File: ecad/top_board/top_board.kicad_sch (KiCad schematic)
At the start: 0 parts

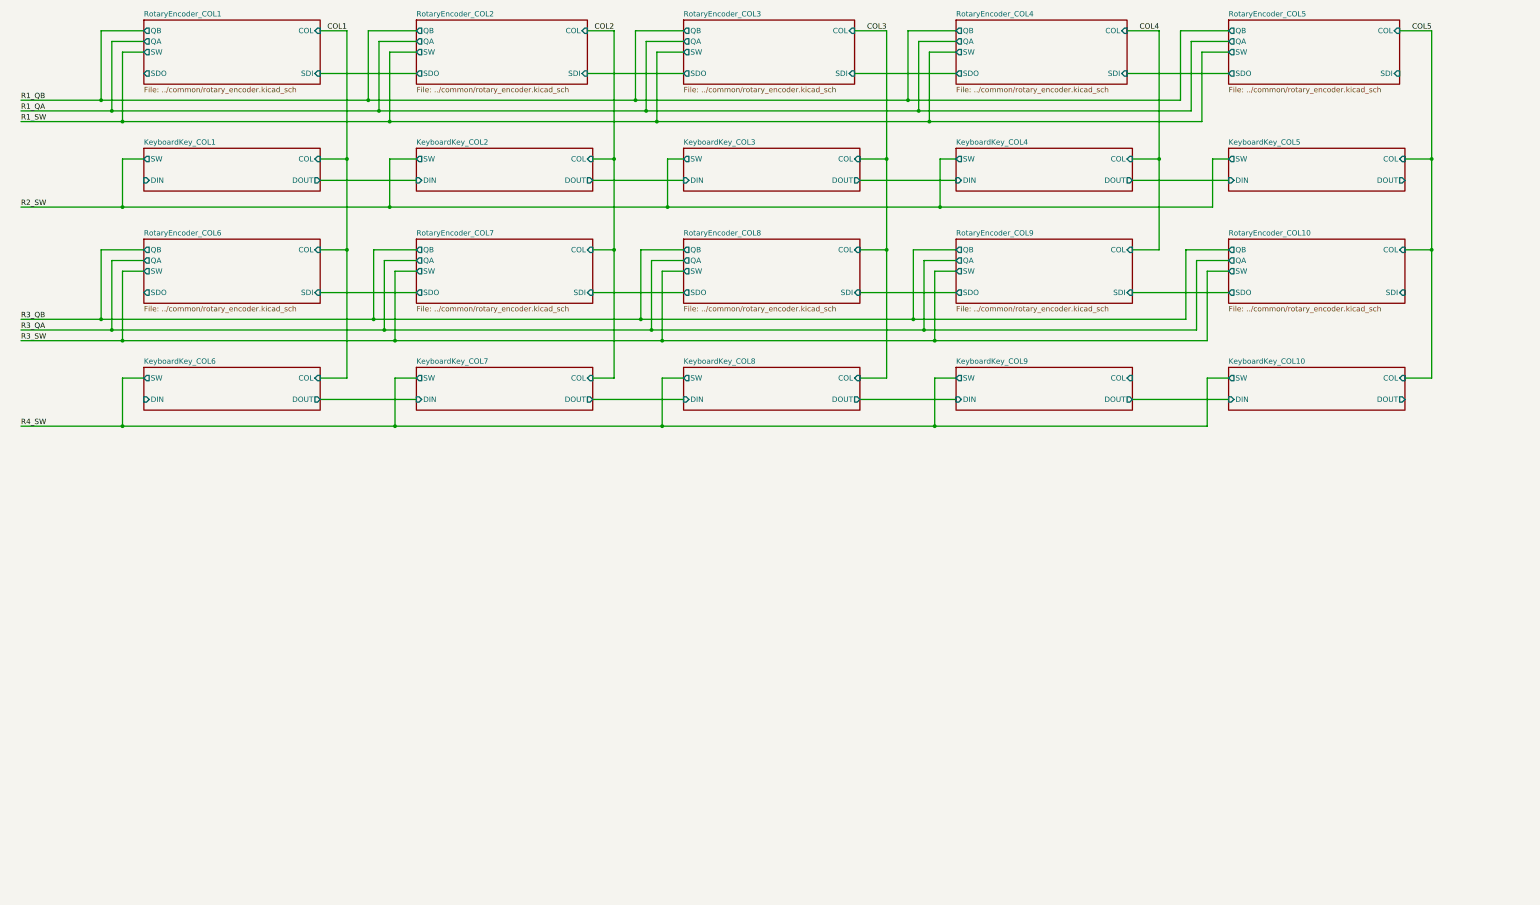
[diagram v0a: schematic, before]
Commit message: Draft a slightly smaller top board
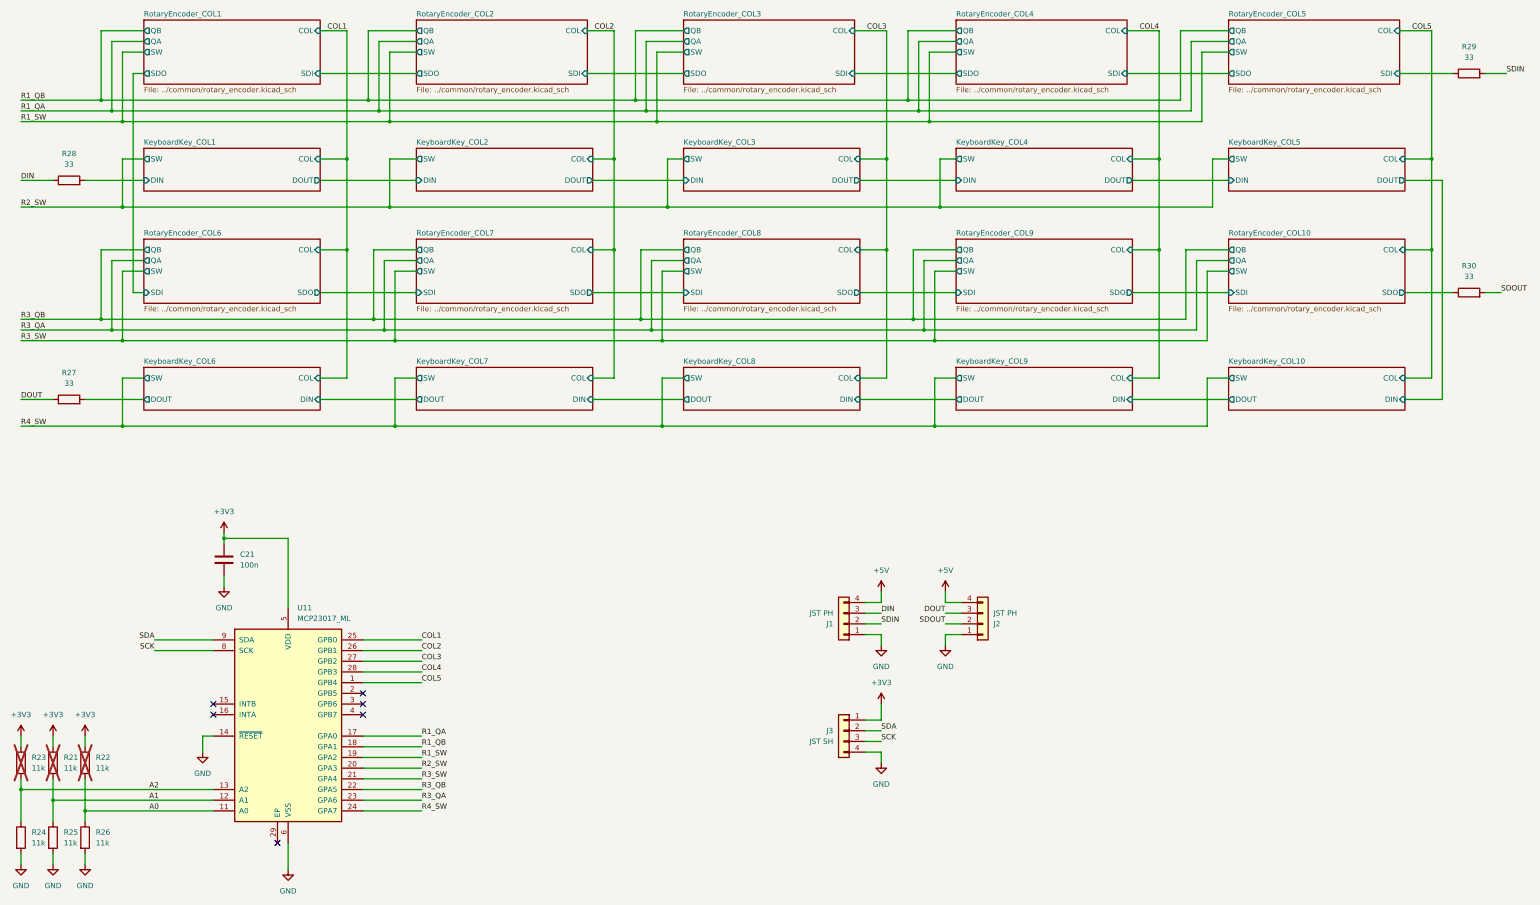
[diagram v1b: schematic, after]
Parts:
- added C21: 100n, Capacitor_SMD:C_0603_1608Metric, symbol Device:C
- added J1, J2: JST PH, Connector_JST:JST_PH_S4B-PH-K_1x04_P2.00mm_Horizontal, symbol Connector_Generic:Conn_01x04
- added J3: JST SH, Connector_JST:JST_SH_BM04B-SRSS-TB_1x04-1MP_P1.00mm_Vertical, symbol Connector_Generic:Conn_01x04
- added R21, R22, R23, R24, R25, R26: 11k, Resistor_SMD:R_0603_1608Metric, symbol Device:R
- added R27, R28, R29, R30: 33, Resistor_SMD:R_0603_1608Metric, symbol Device:R
- added U11: MCP23017_ML, Package_DFN_QFN:QFN-28-1EP_6x6mm_P0.65mm_EP4.25x4.25mm, symbol Interface_Expansion:MCP23017_ML
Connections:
- net COL1: now also U11.25 (GPB0)
- net COL2: now also U11.26 (GPB1)
- net COL3: now also U11.27 (GPB2)
- net COL4: now also U11.28 (GPB3)
- net COL5: now also U11.1 (GPB4)
- net KeyboardKey_COL1/DIN: now also R28.2
- net KeyboardKey_COL6/DOUT: now also R27.2
- net R1_QA: now also U11.17 (GPA0)
- net R1_QB: now also U11.18 (GPA1)
- net R1_SW: now also U11.19 (GPA2)
- net R2_SW: now also U11.20 (GPA3)
- net R3_QA: now also U11.23 (GPA6)
- net R3_QB: now also U11.22 (GPA5)
- net R3_SW: now also U11.21 (GPA4)
- net R4_SW: now also U11.24 (GPA7)
- net RotaryEncoder_COL10/SDO: now also R30.1
- net RotaryEncoder_COL5/SDI: now also R29.1
- new net +3V3: C21.1, J3.1 (Pin_1), R21.1, R22.1, R23.1, U11.5 (VDD)
- new net +5V: J1.4 (Pin_4), J2.4 (Pin_4)
- new net A0: R22.2, R26.1, U11.11 (A0)
- new net A1: R21.2, R25.1, U11.12 (A1)
- new net A2: R23.2, R24.1, U11.13 (A2)
- new net DIN: J1.3 (Pin_3), R28.1
- new net DOUT: J2.3 (Pin_3), R27.1
- new net GND: C21.2, J1.1 (Pin_1), J2.1 (Pin_1), J3.4 (Pin_4), R24.2, R25.2, R26.2, U11.14 (~{RESET}), U11.6 (VSS)
- new net SCK: J3.3 (Pin_3), U11.8 (SCK)
- new net SDA: J3.2 (Pin_2), U11.9 (SDA)
- new net SDIN: J1.2 (Pin_2), R29.2
- new net SDOUT: J2.2 (Pin_2), R30.2
- no-connect marks 0 -> 6
